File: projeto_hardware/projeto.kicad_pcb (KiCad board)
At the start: 2 copper layers, 163 x 75.8 mm, 109 parts, among them J1 arrego, J3 Conn_01x10_Pin, P1 Card_SD, Q1 BC847, Q2 BC847, SW1 BOOT, SW2 BTN2, SW3 RST, SW5 BTN1, SW6 SW_DPDT_x2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

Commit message: pronto - só revisar com calma
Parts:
- removed D8: LED, Resistor_SMD:R_0805_2012Metric_Pad1.20x1.40mm_HandSolder
- removed R32: 220, Resistor_SMD:R_0805_2012Metric_Pad1.20x1.40mm_HandSolder
- removed TP1: TP_12v, TestPoint:TestPoint_Pad_D1.0mm
- removed TP12: TP_IN1_E, TestPoint:TestPoint_Pad_D1.0mm
- removed TP13: TP_IN2_E, TestPoint:TestPoint_Pad_D1.0mm
- removed TP14: TP_IN2_D, TestPoint:TestPoint_Pad_D1.0mm
- removed TP15: TP_IN1_D, TestPoint:TestPoint_Pad_D1.0mm
- removed TP2: TP_GND, TestPoint:TestPoint_Pad_D1.0mm
- removed TP23: TP_SE, TestPoint:TestPoint_Pad_D1.0mm
- removed TP24: TP_SD, TestPoint:TestPoint_Pad_D1.0mm
- removed TP3: TP_3.3V, TestPoint:TestPoint_Pad_D1.0mm
- removed TP4: TP_5V, TestPoint:TestPoint_Pad_D1.0mm
- removed TP5: TP_ME1, TestPoint:TestPoint_Pad_D1.0mm
- removed TP6: TP_ME2, TestPoint:TestPoint_Pad_D1.0mm
- removed TP7: TP_MD1, TestPoint:TestPoint_Pad_D1.0mm
- removed TP8: TP_MD2, TestPoint:TestPoint_Pad_D1.0mm
- removed TP9: TP_VM, TestPoint:TestPoint_Pad_D1.0mm
- added J2: arrego, Connector_PinHeader_2.54mm:PinHeader_1x01_P2.54mm_Vertical, F.Cu at (139.2, 140.0)
- added J4: arrego, Connector_PinHeader_2.54mm:PinHeader_1x01_P2.54mm_Vertical, F.Cu at (139.2, 131.2)
- added J5: arrego, Connector_PinHeader_2.54mm:PinHeader_1x01_P2.54mm_Vertical, F.Cu at (139.2, 128.8)
- moved TP11 8.54 mm to (155.2, 120.8)
- moved TP17 5.76 mm to (158.0, 108.0)
- moved TP19 4.86 mm to (162.5, 108.0)
- moved TP16 4.51 mm to (111.8, 124.2)
- moved TP10 2.92 mm to (141.2, 120.8)
- moved D4 2.85 mm to (189.0, 133.0)
- moved D5 2.85 mm to (189.0, 135.8)
- moved R12 2.80 mm to (193.5, 133.0)
- moved R17 2.70 mm to (193.5, 135.8)
- moved J1 1.82 mm to (115.0, 123.2)
- moved con1 1.25 mm to (101.2, 139.8)
- moved TP21 1.18 mm to (155.8, 108.0)
- moved TP29 0.90 mm to (145.0, 102.8)
- moved TP18 0.51 mm to (160.2, 108.0)
- moved U11 0.39 mm to (149.5, 109.2), turned to 0 degrees
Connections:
- U1 pad 15: IN2_D -> IN1_D
- U1 pad 17: IN1_D -> IN2_D
- U1 pad 30: unconnected-(U1-SPIDQS/GPIO37/FSPIQ/SUBSPIQ-Pad30) -> Net-(J5-Pin_1)
- U1 pad 31: unconnected-(U1-GPIO38/FSPIWP/SUBSPIWP-Pad31) -> Net-(J4-Pin_1)
- U1 pad 39: unconnected-(U1-GPIO1/TOUCH1/ADC1_CH0-Pad39) -> Net-(J2-Pin_1)
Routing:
- net +3.3V: track 0.00 -> 468.4 mm, vias 0 -> 8
- net SD_anal: track 0.00 -> 106.6 mm, vias 0 -> 1
- net SE_anal: track 0.00 -> 84.3 mm, vias 0 -> 3
- net Net-(U9B--): track 0.00 -> 80.0 mm, vias 0 -> 2
- net Net-(U9A--): track 0.00 -> 74.1 mm, vias 0 -> 2
- net RX: track 0.00 -> 71.9 mm, vias 0 -> 2
- net TX: track 0.00 -> 65.6 mm, vias 0 -> 2
- net strp_1: track 0.00 -> 64.8 mm, vias 0 -> 3
- net strp_2: track 0.00 -> 52.2 mm, vias 0 -> 3
- net SCL: track 0.00 -> 44.4 mm, vias 0 -> 2
- net SDA: track 0.00 -> 44.2 mm, vias 0 -> 2
- net GND: track 0.00 -> 42.7 mm, vias 0 -> 27
- net Net-(J3-Pin_2): track 0.00 -> 42.1 mm, vias 0 -> 1
- net RST: track 0.00 -> 42.0 mm
- net BOOT: track 0.00 -> 41.8 mm, vias 0 -> 3
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- added copper zone on B.Cu, net GND
- added copper zone on F.Cu, net GND

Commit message: parafuso m2 - div tensao 1/8W
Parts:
- R22, R25: footprint Resistor_SMD:R_1206_3216Metric -> Resistor_SMD:R_0805_2012Metric_Pad1.20x1.40mm_HandSolder
- moved R25 0.79 mm to (110.5, 128.0)
- moved R22 0.26 mm to (110.5, 130.5)
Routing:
- net DIV_TENSAO: track 40.8 -> 39.5 mm
- net GND: vias 27 -> 28
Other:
- outline, holes or cut-outs redrawn

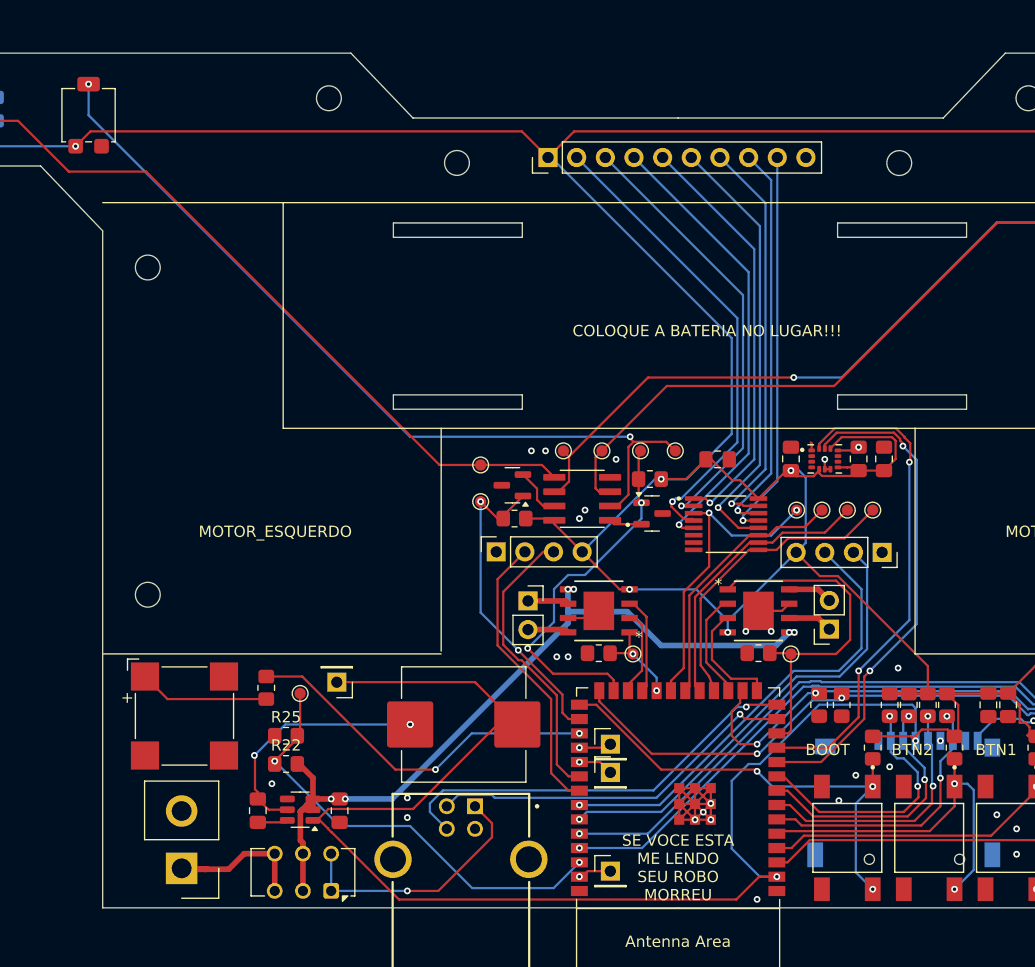
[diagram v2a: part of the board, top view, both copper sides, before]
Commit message: alimentacao 12v perto da bateria
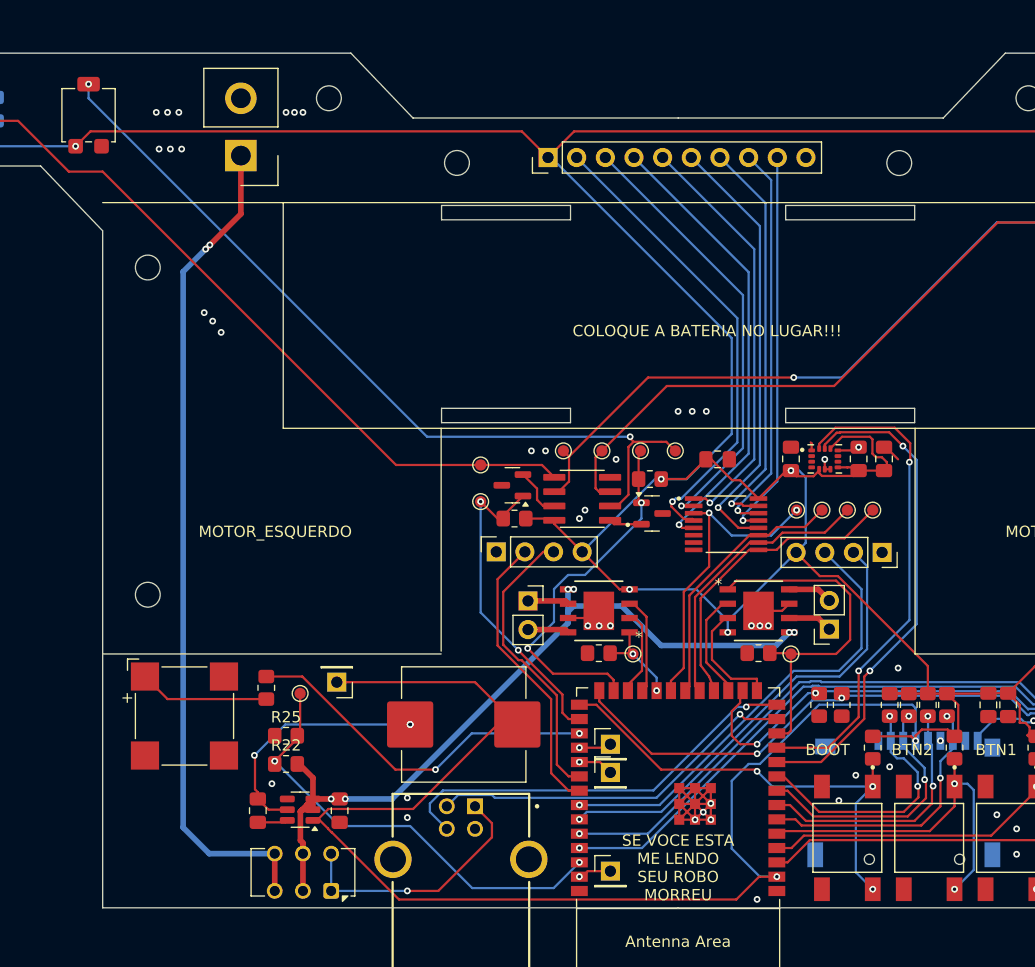
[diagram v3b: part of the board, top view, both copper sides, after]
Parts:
- moved con1 63.4 mm to (106.5, 76.6)
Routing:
- net +12V: track 15.6 -> 74.6 mm, vias 0 -> 2
- net GND: track 42.7 -> 44.4 mm, vias 28 -> 45
- net +3.3V: track 468.4 -> 467.0 mm
- net Net-(U9A--): track 74.1 -> 73.2 mm
- net Vin: track 69.4 -> 70.2 mm
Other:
- outline, holes or cut-outs redrawn

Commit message: projeto step
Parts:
- moved C8 1.68 mm to (149.5, 105.0)
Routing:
- net +3.3V: track 467.0 -> 465.1 mm
- net +12V: track 74.6 -> 73.0 mm
- net GND: track 44.4 -> 45.1 mm
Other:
- outline, holes or cut-outs redrawn
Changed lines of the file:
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@@
 	(footprint "Capacitor_SMD:C_0805_2012Metric_Pad1.18x1.45mm_HandSolder"
 		(layer "F.Cu")
-		(at 148.75 103.5)
+		(at 149.5 105)
 		(descr "Capacitor SMD 0805 (2012 Metric), square (rectangular) end terminal, IPC-7351 nominal with elongated pad for handsoldering. (Body size source: IPC-SM-782 page 76, https://www.pcb-3d.com/wordpress/wp-content/uploads/ipc-sm-782a_amendment_1_and_2.pdf, https://docs.google.com/spreadsheets/d/1BsfQQcO9C6DZCsRaXUlFlo91Tg2WpOkGARC1WS5S8t0/edit?usp=sharing), generated with kicad-footprint-generator")
 		(tags "capacitor handsolder")
@@
 		(layer "Edge.Cuts")
 	)
+	(gr_circle
+		(center 101 138.5)
+		(end 102.5 138.5)
+		(stroke
+			(width 0.05)
+			(type solid)
+		)
+		(fill no)
+		(layer "Edge.Cuts")
+	)
 	(gr_rect
 		(start 124.285 81)
@@
 	)
 	(segment
+		(start 150.03884 105.35)
+		(end 150.745 105.35)
+		(width 0.2)
+		(layer "F.Cu")
+		(net 2)
+	)
+	(segment
 		(start 146.75 135.44)
 		(end 148.15 134.04)
@@
 	)
 	(segment
-		(start 150.745 105.35)
-		(end 152.37 106.975)
+		(start 176.849 121.86484)
+		(end 177.16484 121.549)
 		(width 0.2)
 		(layer "F.Cu")
@@
 	)
 	(segment
-		(start 176.849 121.86484)
-		(end 177.16484 121.549)
+		(start 131 127)
+		(end 127.375 123.375)
 		(width 0.2)
 		(layer "F.Cu")
@@
 	)
 	(segment
-		(start 131 127)
-		(end 127.375 123.375)
+		(start 148.4625 105)
+		(end 148.2125 105.25)
+		(width 0.2)
+		(layer "F.Cu")
+		(net 8)
+	)
+	(segment
+		(start 152.37 106.975)
+		(end 150.4375 106.975)
 		(width 0.2)
 		(layer "F.Cu")
@@
 	)
 	(segment
-		(start 143.75 105.25)
-		(end 145.9625 105.25)
-		(width 0.2)
-		(layer "F.Cu")
-		(net 8)
-	)
-	(segment
 		(start 121.7615 134.4885)
 		(end 114.253468 134.4885)
@@
 	)
 	(segment
-		(start 148.18884 103.5)
-		(end 150.03884 105.35)
+		(start 150.4375 106.975)
+		(end 148.4625 105)
 		(width 0.2)
 		(layer "F.Cu")
@@
 	)
 	(segment
-		(start 145.9625 105.25)
-		(end 147.7125 103.5)
-		(width 0.2)
-		(layer "F.Cu")
-		(net 8)
-	)
-	(segment
 		(start 169.15 127.45)
 		(end 166.85 127.45)
@@
 	)
 	(segment
-		(start 147.7125 103.5)
-		(end 148.18884 103.5)
+		(start 155.71 111.75)
+		(end 157.809 113.849)
 		(width 0.2)
 		(layer "F.Cu")
@@
 	)
 	(segment
-		(start 155.71 111.75)
-		(end 157.809 113.849)
+		(start 175.526 126.85)
+		(end 176.019239 126.85)
 		(width 0.2)
 		(layer "F.Cu")
@@
 	)
 	(segment
-		(start 175.526 126.85)
-		(end 176.019239 126.85)
+		(start 148.2125 105.25)
+		(end 143.75 105.25)
 		(width 0.2)
 		(layer "F.Cu")
@@
 	)
 	(segment
-		(start 150.03884 105.35)
-		(end 150.745 105.35)
-		(width 0.2)
-		(layer "F.Cu")
-		(net 8)
-	)
-	(segment
 		(start 162.5 128.05)
 		(end 165.9 128.05)
@@
 	)
 	(segment
-		(start 151.725 106.975)
-		(end 152.37 106.975)
-		(width 0.2)
-		(layer "F.Cu")
-		(net 8)
-	)
-	(segment
 		(start 134.125 108.75)
 		(end 134.28 108.905)
@@
 	)
 	(segment
-		(start 101.38 136.13)
-		(end 103.7 138.45)
+		(start 101.38 86.87)
+		(end 101.38 133.38)
 		(width 0.5)
 		(layer "B.Cu")
@@
 	)
 	(segment
-		(start 101.38 86.87)
-		(end 101.38 136.13)
+		(start 103.375 84.875)
+		(end 101.38 86.87)
 		(width 0.5)
 		(layer "B.Cu")
@@
 	)
 	(segment
-		(start 103.7 138.45)
-		(end 109.5 138.45)
+		(start 101.38 133.38)
+		(end 106.45 138.45)
 		(width 0.5)
 		(layer "B.Cu")
@@
 	)
 	(segment
-		(start 103.375 84.875)
-		(end 101.38 86.87)
+		(start 106.45 138.45)
+		(end 109.5 138.45)
 		(width 0.5)
 		(layer "B.Cu")

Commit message: projeto step
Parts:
- removed P1: Card_SD, Library:Micro_SD_card
- added J6: MEM2075-00-140-01-A, Library:MEM2075-00-140-01-A_GCT, B.Cu at (167.8, 135.0)
- moved R26 1.81 mm to (170.6, 124.2)
- moved R27 1.81 mm to (167.2, 124.2)
- moved R28 1.81 mm to (165.5, 124.2)
- moved R29 1.81 mm to (168.9, 124.2)
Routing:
- net +3.3V: track 465.1 -> 457.4 mm, vias 8 -> 9
- net MISO: track 24.1 -> 28.3 mm
- net CD: track 8.55 -> 4.70 mm
- net SCK: track 22.9 -> 25.5 mm
- net CS: track 23.0 -> 24.0 mm
- net strp_1: track 64.8 -> 63.9 mm
- net MOSI: track 23.1 -> 23.8 mm
- net strp_2: track 52.2 -> 51.6 mm

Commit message: add resitor 22 ohms no USB
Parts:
- added R32: 22, Resistor_SMD:R_0805_2012Metric_Pad1.20x1.40mm_HandSolder, B.Cu at (132.5, 134.8)
- added R33: 22, Resistor_SMD:R_0805_2012Metric_Pad1.20x1.40mm_HandSolder, B.Cu at (132.5, 132.5)
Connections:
- USB-B-S-X-X-TH1 pad 2: D- -> Net-(USB-B-S-X-X-TH1-D-)
- USB-B-S-X-X-TH1 pad 3: D+ -> Net-(USB-B-S-X-X-TH1-D+)
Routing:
- net D+: track 37.2 -> 23.9 mm
- net Net-(USB-B-S-X-X-TH1-D+): track 0.00 -> 11.7 mm
- net D-: track 33.0 -> 24.3 mm
- net Net-(USB-B-S-X-X-TH1-D-): track 0.00 -> 7.79 mm

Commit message: mandei pros chineses fazerem
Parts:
- moved J4 0.50 mm to (139.2, 131.8)
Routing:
- net BTN_2: track 32.4 -> 30.7 mm
- net Vin: track 70.2 -> 69.2 mm, vias 6 -> 4
- net Net-(J3-Pin_9): track 34.8 -> 35.5 mm, vias 5 -> 2
- net Net-(J4-Pin_1): track 3.13 -> 3.63 mm, vias 1 -> 0
- net Net-(U10-SW): vias 3 -> 2
- net Net-(J5-Pin_1): vias 1 -> 0
- net Net-(J2-Pin_1): vias 1 -> 0
- net (no net): vias 2 -> 0
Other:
- outline, holes or cut-outs redrawn
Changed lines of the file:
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@@
 			(outputformat 1)
 			(mirror no)
-			(drillshape 1)
+			(drillshape 0)
 			(scaleselection 1)
-			(outputdirectory "")
+			(outputdirectory "gerber")
 		)
 	)
@@
 			(at 0 -1.65 0)
 			(layer "F.SilkS")
+			(hide yes)
 			(effects
 				(font
@@
 		)
 		(property "Value" "33k"
-			(at 0 1.65 0)
-			(layer "F.Fab")
+			(at 3 0 0)
+			(layer "F.SilkS")
 			(effects
 				(font
@@
 	(footprint "Connector_PinHeader_2.54mm:PinHeader_1x01_P2.54mm_Vertical"
 		(layer "F.Cu")
-		(at 139.25 131.25)
+		(at 139.25 131.75)
 		(descr "Through hole straight pin header, 1x01, 2.54mm pitch, single row")
 		(tags "Through hole pin header THT 1x01 2.54mm single row")
@@
 			(at 0 -1.65 0)
 			(layer "F.SilkS")
+			(hide yes)
 			(effects
 				(font
@@
 		)
 		(property "Value" "100k"
-			(at 0 1.65 0)
-			(layer "F.Fab")
+			(at 3.75 0 0)
+			(layer "F.SilkS")
 			(effects
 				(font
@@
 			(unlocked yes)
 			(layer "B.SilkS")
+			(hide yes)
 			(effects
 				(font
@@
 			(unlocked yes)
 			(layer "B.Fab")
+			(hide yes)
 			(effects
 				(font
@@
 		(layer "Edge.Cuts")
 	)
+	(gr_circle
+		(center 120.35 90)
+		(end 121.45 90)
+		(stroke
+			(width 0.05)
+			(type solid)
+		)
+		(fill no)
+		(layer "Edge.Cuts")
+	)
 	(gr_line
 		(start 168.75 73.25)
@@
 	)
 	(gr_rect
-		(start 154.785 98.98)
-		(end 166.215 100.25)
+		(start 154.785 98.73)
+		(end 166.215 100)
 		(stroke
 			(width 0.05)
@@
 	)
 	(gr_circle
+		(center 170.25 119)
+		(end 171.35 119)
+		(stroke
+			(width 0.05)
+			(type solid)
+		)
+		(fill no)
+		(layer "Edge.Cuts")
+	)
+	(gr_circle
 		(center 98.25 115.5)
 		(end 99.35 115.5)
@@
 		(layer "Edge.Cuts")
 	)
+	(gr_circle
+		(center 170.25 90)
+		(end 171.35 90)
+		(stroke
+			(width 0.05)
+			(type solid)
+		)
+		(fill no)
+		(layer "Edge.Cuts")
+	)
 	(gr_arc
 		(start 63.75 68.25)
@@
 		(layer "Edge.Cuts")
 	)
+	(gr_circle
+		(center 120.35 119)
+		(end 121.45 119)
+		(stroke
+			(width 0.05)
+			(type solid)
+		)
+		(fill no)
+		(layer "Edge.Cuts")
+	)
 	(gr_line
 		(start 196.25 143.25)
@@
 	)
 	(gr_rect
-		(start 124.285 98.98)
-		(end 135.715 100.25)
+		(start 124.285 98.73)
+		(end 135.715 100)
 		(stroke
 			(width 0.05)
@@
 	)
 	(gr_text "https://github.com/AlisonTristao/bally_robot"
-		(at 163.83 91.44 0)
+		(at 182.25 85.25 90)
 		(layer "B.SilkS")
 		(effects
@@
 	)
 	(gr_text "https://github.com/AlisonTristao/bally_robot"
-		(at 163.83 93.98 0)
+		(at 109.75 87.25 90)
 		(layer "B.SilkS")
 		(effects
@@
 		)
 	)
-	(via
-		(at 203 96.25)
-		(size 0.6)
-		(drill 0.3)
-		(layers "F.Cu" "B.Cu")
-		(net 0)
+	(gr_text "https://github.com/AlisonTristao/bally_robot"
+		(at 163.83 91.44 0)
+		(layer "B.SilkS")
+		(effects
+			(font
+				(size 1 1)
+				(thickness 0.15)
+			)
+			(justify left bottom mirror)
+		)
 	)
-	(via
-		(at 214.75 121.5)
-		(size 0.6)
-		(drill 0.3)
-		(layers "F.Cu" "B.Cu")
-		(net 0)
+	(gr_text "https://github.com/AlisonTristao/bally_robot"
+		(at 163.83 93.98 0)
+		(layer "B.SilkS")
+		(effects
+			(font
+				(size 1 1)
+				(thickness 0.15)
+			)
+			(justify left bottom mirror)
+		)
 	)
 	(segment
@@
 	)
 	(via
-		(at 152.25 142.5)
+		(at 152.5 142)
 		(size 0.6)
 		(drill 0.3)
@@
 		(net 7)
 	)
-	(via
-		(at 121.5 127)
-		(size 0.6)
-		(drill 0.3)
-		(layers "F.Cu" "B.Cu")
-		(net 7)
-	)
 	(segment
 		(start 110.437868 127)
@@
 	)
 	(segment
-		(start 160.224 104.1865)
-		(end 160.25 104.2125)
-		(width 0.2)
-		(layer "F.Cu")
-		(net 8)
-	)
-	(segment
 		(start 160.25 104.2125)
 		(end 160.9625 104.2125)
@@
 		(net 9)
 	)
-	(via
-		(at 136 115.01305)
-		(size 0.6)
-		(drill 0.3)
-		(layers "F.Cu" "B.Cu")
-		(net 9)
-	)
-	(via
-		(at 155.54935 118.8351)
-		(size 0.6)
-		(drill 0.3)
-		(layers "F.Cu" "B.Cu")
-		(net 9)
-	)
 	(segment
 		(start 135.48695 118.01305)
@@
 	)
 	(segment
-		(start 135.48695 115.01305)
-		(end 136 115.01305)
-		(width 0.5)
-		(layer "B.Cu")
-		(net 9)
-	)
-	(segment
 		(start 143.75 120)
 		(end 140.25 116.5)
@@
 	)
 	(segment
-		(start 155.0985 118.8351)
-		(end 155.54935 118.8351)
-		(width 0.5)
-		(layer "B.Cu")
-		(net 9)
-	)
-	(segment
 		(start 138.924374 116.5)
 		(end 138.554472 116.130098)
@@
 	)
 	(segment
+		(start 154.5 77.75)
+		(end 154.5 77.21)
+		(width 0.2)
+		(layer "F.Cu")
+		(net 32)
+	)
+	(segment
 		(start 152.37 108.925)
 		(end 151 108.925)
@@
 		(net 32)
 	)
-	(via
-		(at 154.04 76.75)
-		(size 0.6)
-		(drill 0.3)
-		(layers "F.Cu" "B.Cu")
+	(segment
+		(start 154.5 77.21)
+		(end 154.04 76.75)
+		(width 0.2)
+		(layer "F.Cu")
 		(net 32)
 	)
 	(via
-		(at 154.04 76.75)
+		(at 154.5 77.75)
 		(size 0.6)
 		(drill 0.3)
@@
 	)
 	(via
-		(at 154.04 76.75)
+		(at 151 108.925)
 		(size 0.6)
 		(drill 0.3)
@@
 		(net 32)
 	)
-	(via
-		(at 154.04 76.75)
-		(size 0.6)
-		(drill 0.3)
-		(layers "F.Cu" "B.Cu")
+	(segment
+		(start 154.25 78)
+		(end 154.5 77.75)
+		(width 0.2)
+		(layer "B.Cu")
 		(net 32)
 	)
-	(via
-		(at 151 108.925)
-		(size 0.6)
-		(drill 0.3)
-		(layers "F.Cu" "B.Cu")
+	(segment
+		(start 154.04 78.21)
+		(end 154.04 105.46)
+		(width 0.2)
+		(layer "B.Cu")
 		(net 32)
 	)
 	(segment
-		(start 151 108.5)
-		(end 151 108.925)
+		(start 154.5 77.75)
+		(end 154.04 78.21)
 		(width 0.2)
 		(layer "B.Cu")
@@
 	)
 	(segment
-		(start 154.04 105.46)
-		(end 151 108.5)
+		(start 151 108.5)
+		(end 151 108.925)
 		(width 0.2)
 		(layer "B.Cu")
@@
 	)
 	(segment
-		(start 154.04 76.75)
-		(end 154.04 105.46)
+		(start 154.04 105.46)
+		(end 151 108.5)
 		(width 0.2)
 		(layer "B.Cu")
@@
 	)
 	(segment
-		(start 170.894206 132.25)
-		(end 171.45404 132.809834)
+		(start 170.25 141.1)
+		(end 169.75 141.6)
 		(width 0.2)
 		(layer "B.Cu")
@@
 	(segment
 		(start 169.75 132.25)
-		(end 170.894206 132.25)
+		(end 170.25 132.75)
 		(width 0.2)
 		(layer "B.Cu")
@@
 	)
 	(segment
-		(start 171.45404 139.89596)
-		(end 169.75 141.6)
-		(width 0.2)
-		(layer "B.Cu")
-		(net 56)
-	)
-	(segment
-		(start 171.45404 132.809834)
-		(end 171.45404 139.89596)
+		(start 170.25 132.75)
+		(end 170.25 141.1)
 		(width 0.2)
 		(layer "B.Cu")
@@
 		(net 73)
 	)
-	(via
-		(at 136.5 140.49)
-		(size 0.6)
-		(drill 0.3)
-		(layers "F.Cu" "B.Cu")
-		(net 73)
-	)
 	(segment
 		(start 151.168949 126.52)
@@
 		(net 75)
 	)
-	(via
-		(at 136.5 130.33)
-		(size 0.6)
-		(drill 0.3)
-		(layers "F.Cu" "B.Cu")
+	(segment
+		(start 139.25 131.25)
+		(end 139.25 131.75)
+		(width 0.2)
+		(layer "F.Cu")
 		(net 75)
 	)
@@
 		(net 76)
 	)
-	(via
-		(at 136.5 129.06)
-		(size 0.6)
-		(drill 0.3)
-		(layers "F.Cu" "B.Cu")
-		(net 76)
-	)
 	(segment
 		(start 161.75 126.5)
@@
 	)
 	(group ""
+		(members "19f16eb5-6165-497a-a85f-71d711b17a33" "ac494818-97fa-4ebe-91e1-d98169bf6079")
+	)
+	(group ""
+		(members "6f0584f1-315f-430a-afa2-1841d799340d" "833d05de-8d6e-496e-af8c-74586e87533a")
+	)
+	(group ""
